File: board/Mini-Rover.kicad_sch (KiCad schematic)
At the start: 13 parts, among them IC1 NCP51313ADR2G, U2 OKI, U3 OKI

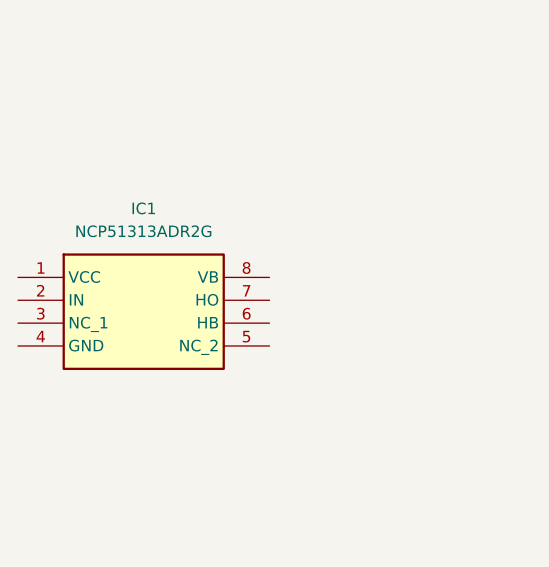
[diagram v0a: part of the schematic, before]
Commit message: Add Gate Driver Circuit
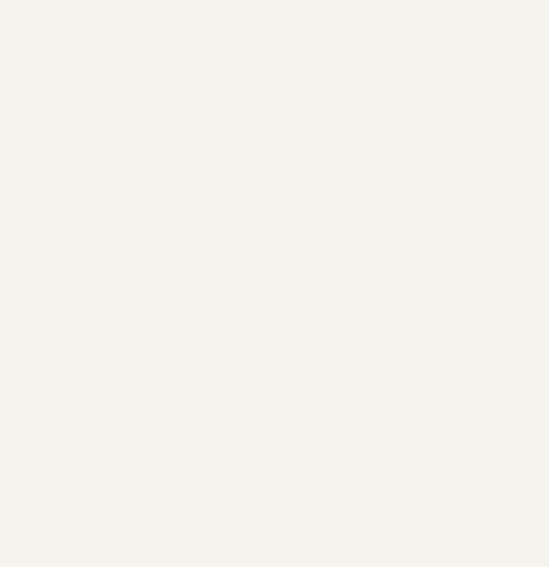
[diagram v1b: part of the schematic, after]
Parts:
- removed IC1: NCP51313ADR2G, SOIC127P600X175-8N, symbol NCP51313ADR2G:NCP51313ADR2G
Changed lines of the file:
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@@
-	)
-	(symbol
-		(lib_id "NCP51313ADR2G:NCP51313ADR2G")
-		(at 59.69 62.23 0)
-		(unit 1)
-		(exclude_from_sim no)
-		(in_bom yes)
-		(on_board yes)
-		(dnp no)
-		(fields_autoplaced yes)
-		(property "Reference" "IC1"
-			(at 73.66 54.61 0)
-			(effects
-				(font
-					(size 1.27 1.27)
-				)
-			)
-		)
-		(property "Value" "NCP51313ADR2G"
-			(at 73.66 57.15 0)
-			(effects
-				(font
-					(size 1.27 1.27)
-				)
-			)
-		)
-		(property "Footprint" "SOIC127P600X175-8N"
-			(at 83.82 157.15 0)
-			(effects
-				(font
-					(size 1.27 1.27)
-				)
-				(justify left top)
-				(hide yes)
-			)
-		)
-		(property "Datasheet" "https://www.onsemi.com/pub/Collateral/NCP51313-D.PDF"
-			(at 83.82 257.15 0)
-			(effects
-				(font
-					(size 1.27 1.27)
-				)
-				(justify left top)
-				(hide yes)
-			)
-		)
-		(property "Description" "2.0 A / 3.0 A Current Capability; Very fast propagation delay (typ. 20 ns for B version); High dv/dt immunity up to 50 V/ns and negative transient immunity"
-			(at 59.69 62.23 0)
-			(effects
-				(font
-					(size 1.27 1.27)
-				)
-				(hide yes)
-			)
-		)
-		(property "Height" "1.75"
-			(at 83.82 457.15 0)
-			(effects
-				(font
-					(size 1.27 1.27)
-				)
-				(justify left top)
-				(hide yes)
-			)
-		)
-		(property "Mouser Part Number" ""
-			(at 83.82 557.15 0)
-			(effects
-				(font
-					(size 1.27 1.27)
-				)
-				(justify left top)
-				(hide yes)
-			)
-		)
-		(property "Mouser Price/Stock" ""
-			(at 83.82 657.15 0)
-			(effects
-				(font
-					(size 1.27 1.27)
-				)
-				(justify left top)
-				(hide yes)
-			)
-		)
-		(property "Manufacturer_Name" "onsemi"
-			(at 83.82 757.15 0)
-			(effects
-				(font
-					(size 1.27 1.27)
-				)
-				(justify left top)
-				(hide yes)
-			)
-		)
-		(property "Manufacturer_Part_Number" "NCP51313ADR2G"
-			(at 83.82 857.15 0)
-			(effects
-				(font
-					(size 1.27 1.27)
-				)
-				(justify left top)
-				(hide yes)
-			)
-		)
-		(pin "4"
-		)
-		(pin "5"
-		)
-		(pin "8"
-		)
-		(pin "3"
-		)
-		(pin "6"
-		)
-		(pin "7"
-		)
-		(pin "1"
-		)
-		(pin "2"
-		)
-		(instances
-			(project ""
-				(path "/fbd9c71c-f200-4aab-a303-9f269bc9de13/fd366cf6-4ba4-4d0b-8257-15ce8ef3829f"
-					(reference "IC1")
-					(unit 1)
-				)
-			)
-		)
 	)
 	(symbol

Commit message: Need different mosfet/gate driver
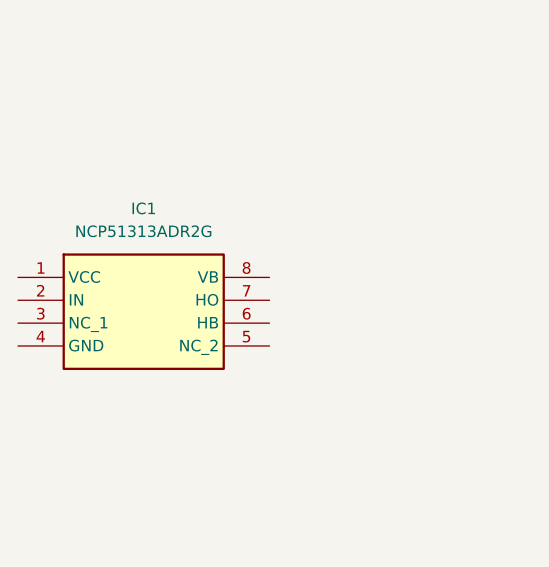
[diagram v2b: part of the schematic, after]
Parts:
- added IC1: NCP51313ADR2G, SOIC127P600X175-8N, symbol NCP51313ADR2G:NCP51313ADR2G
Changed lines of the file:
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@@
+	)
+	(symbol
+		(lib_id "NCP51313ADR2G:NCP51313ADR2G")
+		(at 59.69 62.23 0)
+		(unit 1)
+		(exclude_from_sim no)
+		(in_bom yes)
+		(on_board yes)
+		(dnp no)
+		(fields_autoplaced yes)
+		(property "Reference" "IC1"
+			(at 73.66 54.61 0)
+			(effects
+				(font
+					(size 1.27 1.27)
+				)
+			)
+		)
+		(property "Value" "NCP51313ADR2G"
+			(at 73.66 57.15 0)
+			(effects
+				(font
+					(size 1.27 1.27)
+				)
+			)
+		)
+		(property "Footprint" "SOIC127P600X175-8N"
+			(at 83.82 157.15 0)
+			(effects
+				(font
+					(size 1.27 1.27)
+				)
+				(justify left top)
+				(hide yes)
+			)
+		)
+		(property "Datasheet" "https://www.onsemi.com/pub/Collateral/NCP51313-D.PDF"
+			(at 83.82 257.15 0)
+			(effects
+				(font
+					(size 1.27 1.27)
+				)
+				(justify left top)
+				(hide yes)
+			)
+		)
+		(property "Description" "2.0 A / 3.0 A Current Capability; Very fast propagation delay (typ. 20 ns for B version); High dv/dt immunity up to 50 V/ns and negative transient immunity"
+			(at 59.69 62.23 0)
+			(effects
+				(font
+					(size 1.27 1.27)
+				)
+				(hide yes)
+			)
+		)
+		(property "Height" "1.75"
+			(at 83.82 457.15 0)
+			(effects
+				(font
+					(size 1.27 1.27)
+				)
+				(justify left top)
+				(hide yes)
+			)
+		)
+		(property "Mouser Part Number" ""
+			(at 83.82 557.15 0)
+			(effects
+				(font
+					(size 1.27 1.27)
+				)
+				(justify left top)
+				(hide yes)
+			)
+		)
+		(property "Mouser Price/Stock" ""
+			(at 83.82 657.15 0)
+			(effects
+				(font
+					(size 1.27 1.27)
+				)
+				(justify left top)
+				(hide yes)
+			)
+		)
+		(property "Manufacturer_Name" "onsemi"
+			(at 83.82 757.15 0)
+			(effects
+				(font
+					(size 1.27 1.27)
+				)
+				(justify left top)
+				(hide yes)
+			)
+		)
+		(property "Manufacturer_Part_Number" "NCP51313ADR2G"
+			(at 83.82 857.15 0)
+			(effects
+				(font
+					(size 1.27 1.27)
+				)
+				(justify left top)
+				(hide yes)
+			)
+		)
+		(pin "4"
+		)
+		(pin "5"
+		)
+		(pin "8"
+		)
+		(pin "3"
+		)
+		(pin "6"
+		)
+		(pin "7"
+		)
+		(pin "1"
+		)
+		(pin "2"
+		)
+		(instances
+			(project ""
+				(path "/fbd9c71c-f200-4aab-a303-9f269bc9de13/fd366cf6-4ba4-4d0b-8257-15ce8ef3829f"
+					(reference "IC1")
+					(unit 1)
+				)
+			)
+		)
 	)
 	(symbol
